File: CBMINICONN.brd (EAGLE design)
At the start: 46 x 15 mm, 8 parts

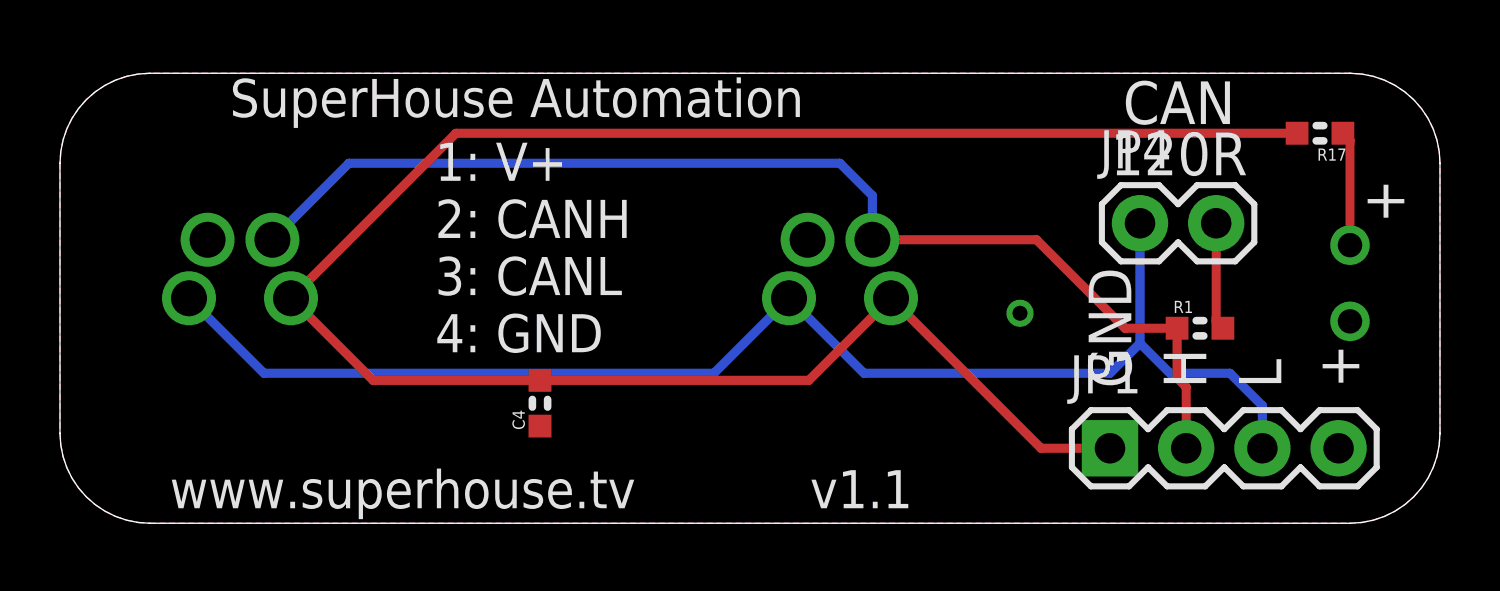
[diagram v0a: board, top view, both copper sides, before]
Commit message: Removed 120R termination, rotated connectors by 20 degrees, and added circular cut-out
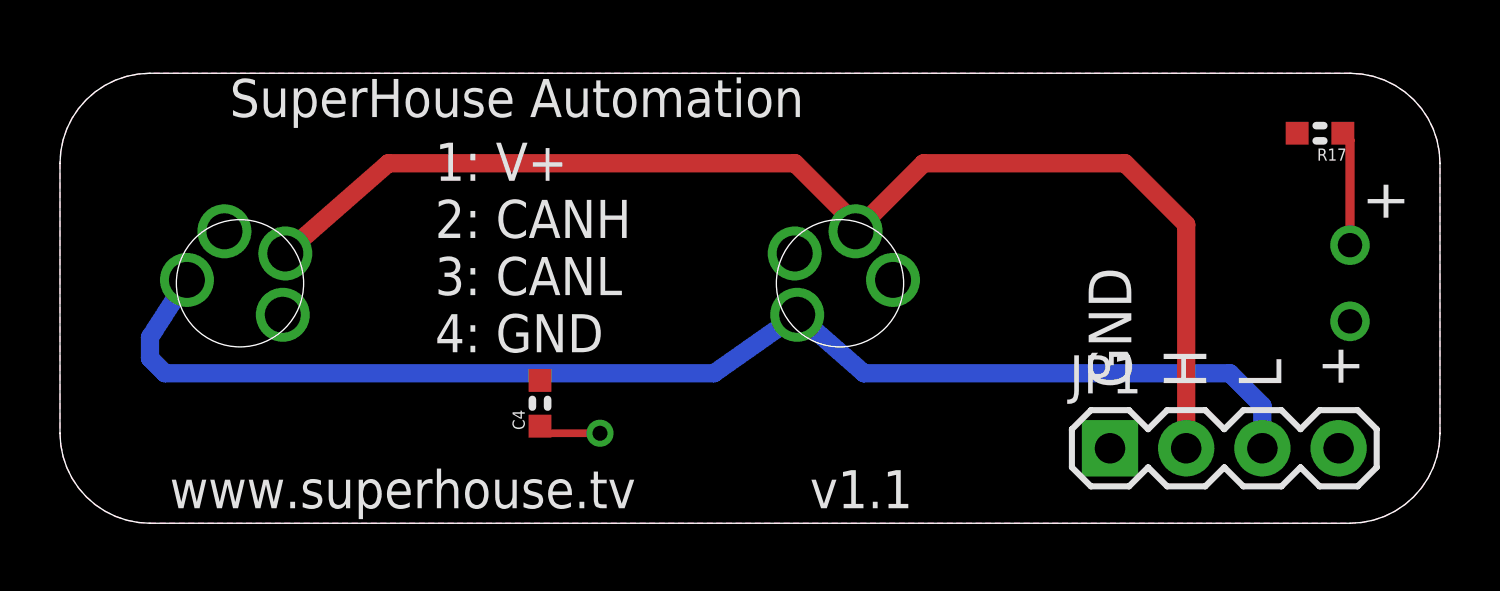
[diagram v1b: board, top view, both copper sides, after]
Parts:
- removed JP4: TERM, freetronics-jon:1X02
- removed R1: 120R, freetronics-master-v1.1:0603
- turned JP2 to 20 degrees
- turned JP3 to 340 degrees
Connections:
- removed net N$3: JP4.2, R1.2
- net CANH: no longer R1.1
- net CANL: no longer JP4.1
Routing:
- net VCC: track 67.5 -> 0.00 mm
- net N$3: track 3.59 -> 0.00 mm
- net CANH: track 38.5 -> 41.5 mm
- net CANL: track 45.6 -> 43.5 mm
- net GND: track 0.00 -> 2.10 mm
- added copper zone on layer 1, net VCC
- removed copper zone on layer 1, net GND
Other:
- outline, holes or cut-outs redrawn
- board text removed: "CAN 120R"

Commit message: Clearance for connectors
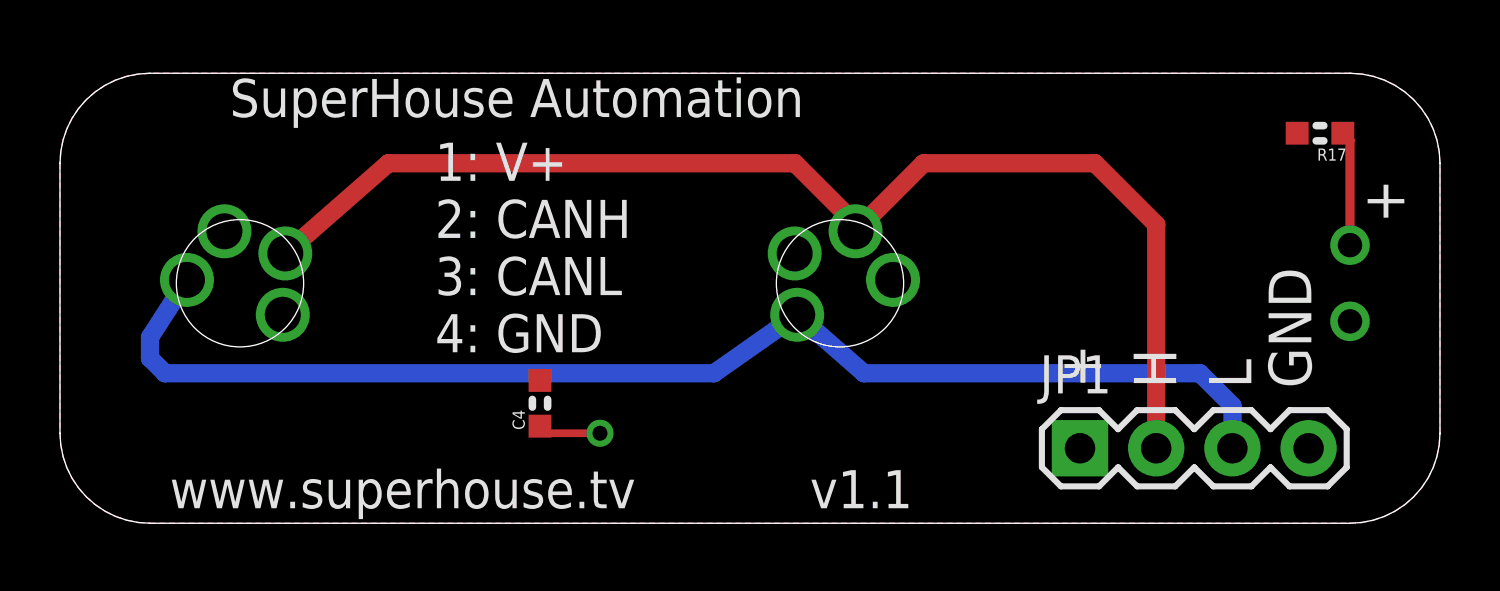
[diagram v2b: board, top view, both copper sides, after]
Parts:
- moved JP1 1.00 mm to (34.0, 2.50)
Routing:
- net CANL: track 43.5 -> 42.5 mm
- net CANH: track 41.5 -> 40.5 mm
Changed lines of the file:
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@@
 <dimension x1="46" y1="16" x2="0" y2="16" x3="23" y3="18.000003125" textsize="1.778" layer="47"/>
 <dimension x1="47" y1="0" x2="47" y2="15" x3="48.999996875" y3="7.5" textsize="1.778" layer="47"/>
-<text x="42.6" y="4.5" size="1.4224" layer="21" font="vector" ratio="16" rot="R90" align="center-left">+</text>
-<text x="37.5" y="4.5" size="1.4224" layer="21" font="vector" ratio="16" rot="R90" align="center-left">H</text>
-<text x="40" y="4.5" size="1.4224" layer="21" font="vector" ratio="16" rot="R90" align="center-left">L</text>
-<text x="35" y="4.5" size="1.4224" layer="21" font="vector" ratio="16" rot="R90" align="center-left">GND</text>
+<text x="34" y="4.5" size="1.4224" layer="21" font="vector" ratio="16" rot="R90" align="center-left">+</text>
+<text x="36.5" y="4.5" size="1.4224" layer="21" font="vector" ratio="16" rot="R90" align="center-left">H</text>
+<text x="39" y="4.5" size="1.4224" layer="21" font="vector" ratio="16" rot="R90" align="center-left">L</text>
+<text x="41" y="4.5" size="1.4224" layer="21" font="vector" ratio="16" rot="R90" align="center-left">GND</text>
 <text x="12.5" y="5.7" size="1.27" layer="21" font="vector" ratio="16">1: V+
 2: CANH
@@
 <attribute name="VALUE" x="40.984" y="11.0348" size="1.016" layer="27" font="vector"/>
 </element>
-<element name="JP1" library="freetronics-jon" package="1X04" value="CAN" x="35" y="2.5" smashed="yes">
-<attribute name="NAME" x="33.6538" y="4.3288" size="1.27" layer="25" ratio="10"/>
-<attribute name="VALUE" x="30.23" y="1.825" size="1.27" layer="27" font="vector"/>
+<element name="JP1" library="freetronics-jon" package="1X04" value="CAN" x="34" y="2.5" smashed="yes">
+<attribute name="NAME" x="32.6538" y="4.3288" size="1.27" layer="25" ratio="10"/>
+<attribute name="VALUE" x="29.23" y="1.825" size="1.27" layer="27" font="vector"/>
 </element>
 <element name="LED1" library="freetronics-jon" package="LED3MM" value="GREEN" x="43" y="8" smashed="yes" rot="MR270">
@@
 <wire x1="26.518940625" y1="9.731934375" x2="26.518940625" y2="9.981059375" width="0.6096" layer="1"/>
 <wire x1="28.78700625" y1="12" x2="26.518940625" y2="9.731934375" width="0.6096" layer="1"/>
-<wire x1="37.54" y1="2.5" x2="37.54" y2="9.96" width="0.6096" layer="1"/>
-<wire x1="37.54" y1="9.96" x2="35.5" y2="12" width="0.6096" layer="1"/>
-<wire x1="35.5" y1="12" x2="28.78700625" y2="12" width="0.6096" layer="1"/>
+<wire x1="36.54" y1="2.5" x2="36.54" y2="9.96" width="0.6096" layer="1"/>
+<wire x1="36.54" y1="9.96" x2="34.5" y2="12" width="0.6096" layer="1"/>
+<wire x1="34.5" y1="12" x2="28.78700625" y2="12" width="0.6096" layer="1"/>
 </signal>
 <signal name="CANL">
@@
 <wire x1="24.573534375" y1="6.94871875" x2="21.8" y2="5" width="0.6096" layer="16"/>
 <wire x1="24.573534375" y1="6.94871875" x2="26.8" y2="5" width="0.6096" layer="16"/>
-<wire x1="39" y1="5" x2="40.08" y2="3.92" width="0.6096" layer="16"/>
-<wire x1="40.08" y1="3.92" x2="40.08" y2="2.5" width="0.6096" layer="16"/>
+<wire x1="38" y1="5" x2="39.08" y2="3.92" width="0.6096" layer="16"/>
+<wire x1="39.08" y1="3.92" x2="39.08" y2="2.5" width="0.6096" layer="16"/>
 <wire x1="3.5" y1="5" x2="3" y2="5.5" width="0.6096" layer="16"/>
 <wire x1="21.8" y1="5" x2="3.5" y2="5" width="0.6096" layer="16"/>
 <wire x1="3" y1="5.5" x2="3" y2="6.2" width="0.6096" layer="16"/>
 <wire x1="3" y1="6.2" x2="4.2315125" y2="8.1115875" width="0.6096" layer="16"/>
-<wire x1="26.8" y1="5" x2="39" y2="5" width="0.6096" layer="16"/>
+<wire x1="26.8" y1="5" x2="38" y2="5" width="0.6096" layer="16"/>
 </signal>
 <signal name="N$1">
